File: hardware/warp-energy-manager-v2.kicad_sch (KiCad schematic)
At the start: 120 parts, among them J101 Boot, J102 DM3CS, P101 CON-SENSOR2, P102 SG-Ready, P103 L+N, P104 OUT, P105 INPUT, P110 MODBUS, P111 Debug, Q101 2N7002P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

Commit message: routing started
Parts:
- removed D101, D105, D107, D112: B0520LW-7, kicad-libraries:SOD-123, symbol tinkerforge:DIODESCH
- removed D104, D110: blue, kicad-libraries:D0603E, symbol tinkerforge:LED
- removed Q102, Q107: SSM6N7002KFU, kicad-libraries:SOT363, symbol tinkerforge:DUAL_MOSFET_N_CH
- removed R103, R114: 1k, kicad-libraries:R0603F, symbol tinkerforge:R
- removed RP105: 10k, kicad-libraries:4X0603, symbol tinkerforge:R_PACK4
- removed U105, U109: HCPL2731, kicad-libraries:DIP-8, symbol tinkerforge:HCPL-2731-000E
- added D101, D104, D105: LL4148, kicad-libraries:MiniMelf, symbol tinkerforge:DIODE
- added Q102, Q107: 2N7002P, kicad-libraries:SOT23GDS, symbol tinkerforge:MOSFET_N_CH
- added U106: IS2805-4, kicad-libraries:SOIC16_44, symbol tinkerforge:LTV-847
- C105: value 100uF -> 2.2uF; footprint kicad-libraries:C1210 -> kicad-libraries:C0603F
- P104: footprint kicad-libraries:OQ_4P_5mm -> kicad-libraries:OQ_4P_5mm_230V
- R101: value 1k -> 10k; footprint kicad-libraries:R1206E -> kicad-libraries:R0603F
- R102, R118: value 1k -> 10k
- R104, R105, R112, R115, R116, R117, R120, R121: footprint kicad-libraries:R1206E -> kicad-libraries:R0805E
- R110, R113: footprint kicad-libraries:R0402F -> kicad-libraries:R0603F
- U104: footprint (none) -> kicad-libraries:SOT25
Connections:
- net 3V3: now also RP104.2 (P2), RP104.3 (P3)
- net GND: now also D105.2 (K), Q102.S, Q107.S, U106.11, U106.13, U106.15, U106.9
- net IN0: now also RP104.8 (R1), U101.7 (P2.4_AI), U106.16; no longer RP104.2 (P2), U101.9 (P2.6_AI)
- net IN1: now also RP104.7 (R2), U101.8 (P2.5_AI), U106.14; no longer RP104.3 (P3), U101.10 (P2.7_AI)
- net L: now also U102.2 (N); no longer U102.1 (L)
- net N: now also U102.1 (L); no longer U102.2 (N)
- net RELAY0: now also Q107.G
- net RELAY1: now also Q102.G
- net V12: now also U101.6 (P2.3_AI); no longer U101.7 (P2.4_AI)
- net VCC: now also C115.2, D101.2 (K), D104.2 (K)
- net at R124.1: now also U101.12 (P2.9_AI); no longer U101.35 (P0.6_IO)
- net at C114.1, R112.2: now also U106.1
- net at C112.1, R117.2: now also U106.3
- net at L104.5, P110.1 (P1): no longer C115.2
- net at P110.2 (P2), R137.2: now also L104.6; no longer L104.7
- net at P110.3 (P3), R137.1: now also L104.7; no longer L104.6
- net at D111.1 (A), R134.2, R135.1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: now also L104.3; no longer L104.2
- net at D106.1 (A), R135.2, R136.1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: now also L104.2; no longer L104.3
- net at REL101.3: no longer P102.3 (P3)
- net at REL101.4: no longer P102.4 (P4)
- net at REL101.5: now also P102.4 (P4)
- net at REL101.6: now also P102.3 (P3)
- net at Q103.D, REL101.8: now also D104.1 (A)
- net at P102.1 (P1): now also REL102.6; no longer REL102.3
- net at P102.2 (P2): now also REL102.5; no longer REL102.4
- net at C134.1, R120.2: now also U106.5
- net at C124.1, R121.2: now also U106.7
- net IN2: now reaches RP104.6 (R3)
- net IN2: now also U101.9 (P2.6_AI), U106.12; no longer RP104.5 (R4)
- net at D108.1 (A), Q104.A1: now also Q102.D
- net at D109.1 (A), Q106.A1: now also Q107.D
- net at Q101.D, REL102.8: now also D101.1 (A)
- new net: D105.1 (A), U106.2, U106.4, U106.6, U106.8
- new net IN3: RP104.5 (R4), U101.10 (P2.7_AI), U106.10
- no-connect marks 29 -> 26
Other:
- note removed: "25mA max -> @12V -> 480 Ohm"
- moved on the sheet: C104, C107, C112, C113, C114, C115, C116, C122, C123, C124, C133, C134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

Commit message: fix schematic drcs
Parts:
- P111: footprint kicad-libraries:DEBUG_PAD -> kicad-libraries:TSTP_MINI
- U106: footprint kicad-libraries:SOIC16_44 -> DIP-16
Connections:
- net SD-CDS: now also U101.5 (P2.2_AI); no longer U101.4 (P2.1_AIO)
- net SD-EN: now also U101.4 (P2.1_AIO); no longer U101.25 (P1.1_IHO)
- no-connect marks 26 -> 25
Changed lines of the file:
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@@
 	)
 	(no_connect
-		(at 69.85 267.97)
-	)
-	(no_connect
-		(at 133.35 106.68)
+		(at 133.35 121.92)
 	)
 	(no_connect
-		(at 133.35 121.92)
+		(at 50.8 88.9)
 	)
 	(no_connect
@@
 	)
 	(no_connect
-		(at 69.85 265.43)
+		(at 133.35 88.9)
 	)
 	(no_connect
@@
 	)
 	(no_connect
+		(at 133.35 76.2)
+	)
+	(no_connect
 		(at 50.8 83.82)
 	)
@@
 		(at 133.35 148.59)
 	)
-	(no_connect
-		(at 69.85 262.89)
-	)
 	(wire
 		(pts
@@
 	(wire
 		(pts
-			(xy 133.35 104.14) (xy 130.81 104.14)
+			(xy 133.35 106.68) (xy 130.81 106.68)
 		)
 		(stroke
@@
 	(wire
 		(pts
-			(xy 129.54 76.2) (xy 133.35 76.2)
+			(xy 129.54 104.14) (xy 133.35 104.14)
 		)
 		(stroke
@@
 	(global_label "SD-EN"
 		(shape output)
-		(at 129.54 76.2 180)
+		(at 129.54 104.14 180)
 		(fields_autoplaced yes)
 		(effects
@@
 		)
 		(property "Intersheetrefs" "${INTERSHEET_REFS}"
-			(at 122.6274 76.2 0)
+			(at 122.6274 104.14 0)
 			(effects
 				(font
@@
 	(global_label "SD-CDS"
 		(shape input)
-		(at 130.81 104.14 180)
+		(at 130.81 106.68 180)
 		(fields_autoplaced yes)
 		(effects
@@
 		)
 		(property "Intersheetrefs" "${INTERSHEET_REFS}"
-			(at 122.9069 104.14 0)
+			(at 122.9069 106.68 0)
 			(effects
 				(font
@@
 			)
 		)
-		(property "Description" ""
+		(property "Description" "Connector 01x02"
 			(at 19.05 68.58 0)
 			(effects
@@
 			)
 		)
-		(property "Description" ""
+		(property "Description" "4 resistors Pack"
 			(at 124.46 46.99 0)
 			(effects
@@
 			)
 		)
-		(property "Footprint" "kicad-libraries:DEBUG_PAD"
+		(property "Footprint" "kicad-libraries:TSTP_MINI"
 			(at 43.18 78.74 0)
 			(effects
@@
 			)
 		)
-		(property "Description" ""
+		(property "Description" "Transistor P-MOSFET (general)"
 			(at 99.06 33.02 0)
 			(effects
@@
 			)
 		)
-		(property "Description" ""
+		(property "Description" "Connector 01x04"
 			(at 130.81 251.46 0)
 			(effects
@@
 			)
 		)
-		(property "Description" ""
+		(property "Description" "power-flag symbol"
 			(at 224.79 172.72 0)
 			(effects
@@
 			)
 		)
-		(property "Description" ""
+		(property "Description" "4 resistors Pack"
 			(at 39.37 255.27 0)
 			(effects
@@
 	)
 	(symbol
-		(lib_name "CONN_01X04_1")
 		(lib_id "tinkerforge:CONN_01X04")
 		(at 167.64 114.3 180)
@@
 			)
 		)
-		(property "Description" ""
+		(property "Description" "power-flag symbol"
 			(at 91.44 93.98 0)
 			(effects
@@
 			)
 		)
-		(property "Description" ""
+		(property "Description" "Transistor P-MOSFET, collector connected to mounting plane (general)"
 			(at 232.41 38.1 0)
 			(effects
@@
 			)
 		)
-		(property "Description" ""
+		(property "Description" "power-flag symbol"
 			(at 207.01 39.37 0)
 			(effects
@@
 			)
 		)
-		(property "Description" ""
+		(property "Description" "4 resistors Pack"
 			(at 367.03 219.71 0)
 			(effects
@@
 			)
 		)
-		(property "Description" ""
+		(property "Description" "power-flag symbol"
 			(at 119.38 229.87 0)
 			(effects
@@
 			)
 		)
-		(property "Description" ""
+		(property "Description" "Transistor P-MOSFET, collector connected to mounting plane (general)"
 			(at 302.26 45.72 0)
 			(effects
@@
 	)
 	(symbol
-		(lib_name "CONN_01X04_1")
 		(lib_id "tinkerforge:CONN_01X04")
 		(at 167.64 54.61 180)
@@
 			)
 		)
-		(property "Description" ""
+		(property "Description" "power-flag symbol"
 			(at 100.33 207.01 0)
 			(effects
@@
 			)
 		)
-		(property "Description" ""
+		(property "Description" "power-flag symbol"
 			(at 207.01 78.74 0)
 			(effects
@@
 			)
 		)
-		(property "Footprint" "kicad-libraries:SOIC16_44"
+		(property "Footprint" "DIP-16"
 			(at 266.7 191.4355 0)
 			(effects
@@
 			)
 		)
-		(property "Datasheet" ""
+		(property "Datasheet" "http://www.us.liteon.com/downloads/LTV-817-827-847.PDF"
 			(at 266.7 193.8598 0)
 			(effects
@@
 			)
 		)
-		(property "Description" ""
+		(property "Description" "DIP-16, Quad DC Optocoupler, Vce 35V, CTR 50%"
 			(at 266.7 212.09 0)
 			(effects
@@
 			)
 		)
-		(property "Description" ""
+		(property "Description" "Transistor P-MOSFET, collector connected to mounting plane (general)"
 			(at 302.26 95.25 0)
 			(effects
@@
 			)
 		)
-		(property "Description" ""
+		(property "Description" "Transistor P-MOSFET, collector connected to mounting plane (general)"
 			(at 232.41 77.47 0)
 			(effects
@@
 			)
 		)
-		(property "Description" ""
+		(property "Description" "power-flag symbol"
 			(at 304.8 71.12 0)
 			(effects
@@
 			)
 		)
-		(property "Description" ""
+		(property "Description" "4 resistors Pack"
 			(at 290.83 189.23 0)
 			(effects
@@
 			)
 		)
-		(property "Description" ""
+		(property "Description" "power-flag symbol"
 			(at 304.8 21.59 0)
 			(effects
@@
 			)
 		)
-		(property "Description" ""
+		(property "Description" "power-flag symbol"
 			(at 224.79 218.44 0)
 			(effects

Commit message: fully routed
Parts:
- P111: footprint kicad-libraries:TSTP_MINI -> kicad-libraries:TSTP_STL
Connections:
- net RELAY0: now also U101.24 (P1.2_IHO); no longer U101.22 (P1.4_IHO)
- net RELAY1: now also U101.23 (P1.3_IHO); no longer U101.21 (P1.5_IHO)
- net SG-OUT-0: now also U101.22 (P1.4_IHO); no longer U101.24 (P1.2_IHO)
- net SG-OUT-1: now also U101.21 (P1.5_IHO); no longer U101.23 (P1.3_IHO)
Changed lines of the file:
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@@
 	(global_label "RELAY1"
 		(shape output)
-		(at 129.54 86.36 180)
-		(fields_autoplaced yes)
-		(effects
-			(font
-				(size 0.9906 0.9906)
-			)
-			(justify right)
-		)
-		(property "Intersheetrefs" "${INTERSHEET_REFS}"
-			(at 122.3916 86.36 0)
+		(at 129.54 81.28 180)
+		(fields_autoplaced yes)
+		(effects
+			(font
+				(size 0.9906 0.9906)
+			)
+			(justify right)
+		)
+		(property "Intersheetrefs" "${INTERSHEET_REFS}"
+			(at 122.3916 81.28 0)
 			(effects
 				(font
@@
 	(global_label "SG-OUT-0"
 		(shape output)
-		(at 129.54 78.74 180)
-		(fields_autoplaced yes)
-		(effects
-			(font
-				(size 0.9906 0.9906)
-			)
-			(justify right)
-		)
-		(property "Intersheetrefs" "${INTERSHEET_REFS}"
-			(at 119.5613 78.74 0)
+		(at 129.54 83.82 180)
+		(fields_autoplaced yes)
+		(effects
+			(font
+				(size 0.9906 0.9906)
+			)
+			(justify right)
+		)
+		(property "Intersheetrefs" "${INTERSHEET_REFS}"
+			(at 119.5613 83.82 0)
 			(effects
 				(font
@@
 	(global_label "RELAY0"
 		(shape output)
-		(at 129.54 83.82 180)
-		(fields_autoplaced yes)
-		(effects
-			(font
-				(size 0.9906 0.9906)
-			)
-			(justify right)
-		)
-		(property "Intersheetrefs" "${INTERSHEET_REFS}"
-			(at 122.3916 83.82 0)
+		(at 129.54 78.74 180)
+		(fields_autoplaced yes)
+		(effects
+			(font
+				(size 0.9906 0.9906)
+			)
+			(justify right)
+		)
+		(property "Intersheetrefs" "${INTERSHEET_REFS}"
+			(at 122.3916 78.74 0)
 			(effects
 				(font
@@
 	(global_label "SG-OUT-1"
 		(shape output)
-		(at 129.54 81.28 180)
-		(fields_autoplaced yes)
-		(effects
-			(font
-				(size 0.9906 0.9906)
-			)
-			(justify right)
-		)
-		(property "Intersheetrefs" "${INTERSHEET_REFS}"
-			(at 119.5613 81.28 0)
+		(at 129.54 86.36 180)
+		(fields_autoplaced yes)
+		(effects
+			(font
+				(size 0.9906 0.9906)
+			)
+			(justify right)
+		)
+		(property "Intersheetrefs" "${INTERSHEET_REFS}"
+			(at 119.5613 86.36 0)
 			(effects
 				(font
@@
 			)
 		)
-		(property "Footprint" "kicad-libraries:TSTP_MINI"
+		(property "Footprint" "kicad-libraries:TSTP_STL"
 			(at 43.18 78.74 0)
 			(effects

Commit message: all bugs fixed
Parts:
- U106: footprint DIP-16 -> kicad-libraries:SOIC16_44
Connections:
- net at P111.1: now also U101.35 (P0.6_IO); no longer U101.31 (P0.2_IO)
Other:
- moved on the sheet: P111
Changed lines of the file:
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@@
 	)
 	(no_connect
-		(at 50.8 88.9)
+		(at 50.8 78.74)
 	)
 	(no_connect
@@
 	(wire
 		(pts
-			(xy 50.8 78.74) (xy 45.72 78.74)
+			(xy 50.8 88.9) (xy 45.72 88.9)
 		)
 		(stroke
@@
 	(symbol
 		(lib_id "tinkerforge:CONN_1")
-		(at 43.18 78.74 0)
+		(at 43.18 88.9 0)
 		(mirror y)
 		(unit 1)
@@
 		(dnp no)
 		(property "Reference" "P111"
-			(at 49.53 77.47 0)
+			(at 40.64 86.36 0)
 			(effects
 				(font
@@
 		)
 		(property "Value" "Debug"
-			(at 38.1 78.74 0)
+			(at 38.1 88.9 0)
 			(effects
 				(font
@@
 		)
 		(property "Footprint" "kicad-libraries:TSTP_STL"
-			(at 43.18 78.74 0)
+			(at 43.18 88.9 0)
 			(effects
 				(font
@@
 		)
 		(property "Datasheet" ""
-			(at 43.18 78.74 0)
+			(at 43.18 88.9 0)
 			(effects
 				(font
@@
 		)
 		(property "Description" ""
-			(at 43.18 78.74 0)
+			(at 43.18 88.9 0)
 			(effects
 				(font
@@
 			)
 		)
-		(property "Footprint" "DIP-16"
+		(property "Footprint" "kicad-libraries:SOIC16_44"
 			(at 266.7 191.4355 0)
 			(effects
@@
 			)
 		)
-		(property "Datasheet" "http://www.us.liteon.com/downloads/LTV-817-827-847.PDF"
+		(property "Datasheet" ""
 			(at 266.7 193.8598 0)
 			(effects
@@
 			)
 		)
-		(property "Description" "DIP-16, Quad DC Optocoupler, Vce 35V, CTR 50%"
+		(property "Description" ""
 			(at 266.7 212.09 0)
 			(effects

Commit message: add 3d models
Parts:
- R104, R105, R115, R116: value 1k -> 2k2
- R112, R117, R120, R121: value 1k -> 680
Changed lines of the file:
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@@
 			)
 		)
-		(property "Value" "1k"
+		(property "Value" "680"
 			(at 214.63 184.15 90)
 			(effects
@@
 			)
 		)
-		(property "Value" "1k"
+		(property "Value" "680"
 			(at 214.63 191.77 90)
 			(effects
@@
 			)
 		)
-		(property "Value" "1k"
+		(property "Value" "2k2"
 			(at 185.42 199.39 90)
 			(effects
@@
 			)
 		)
-		(property "Value" "1k"
+		(property "Value" "2k2"
 			(at 180.34 199.39 90)
 			(effects
@@
 			)
 		)
-		(property "Value" "1k"
+		(property "Value" "2k2"
 			(at 180.34 245.11 90)
 			(effects
@@
 			)
 		)
-		(property "Value" "1k"
+		(property "Value" "2k2"
 			(at 185.42 245.11 90)
 			(effects
@@
 			)
 		)
-		(property "Value" "1k"
+		(property "Value" "680"
 			(at 214.63 229.87 90)
 			(effects
@@
 			)
 		)
-		(property "Value" "1k"
+		(property "Value" "680"
 			(at 214.63 237.49 90)
 			(effects

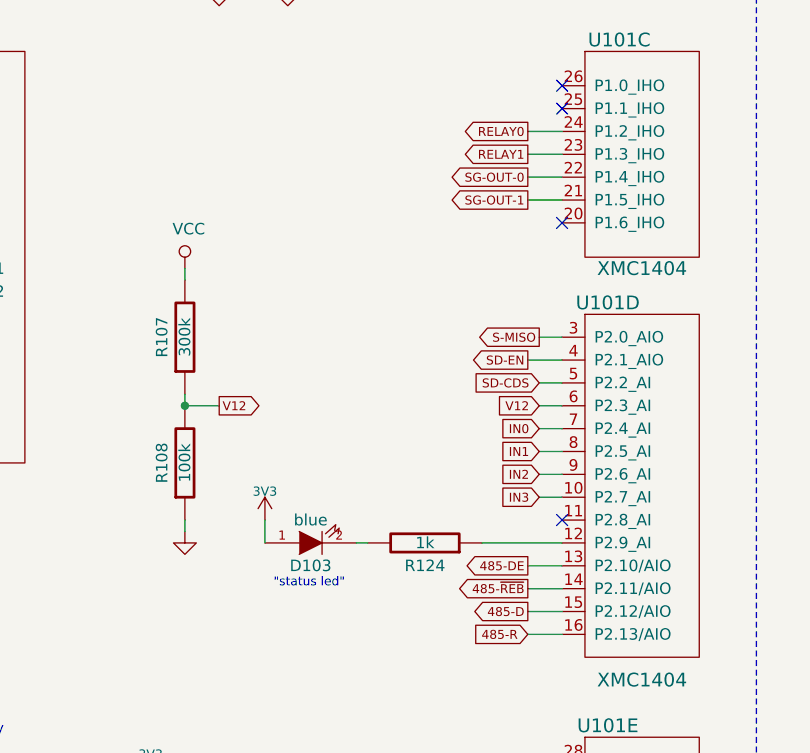
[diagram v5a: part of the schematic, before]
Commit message: add version 2.1: fix varistor space, fix status led
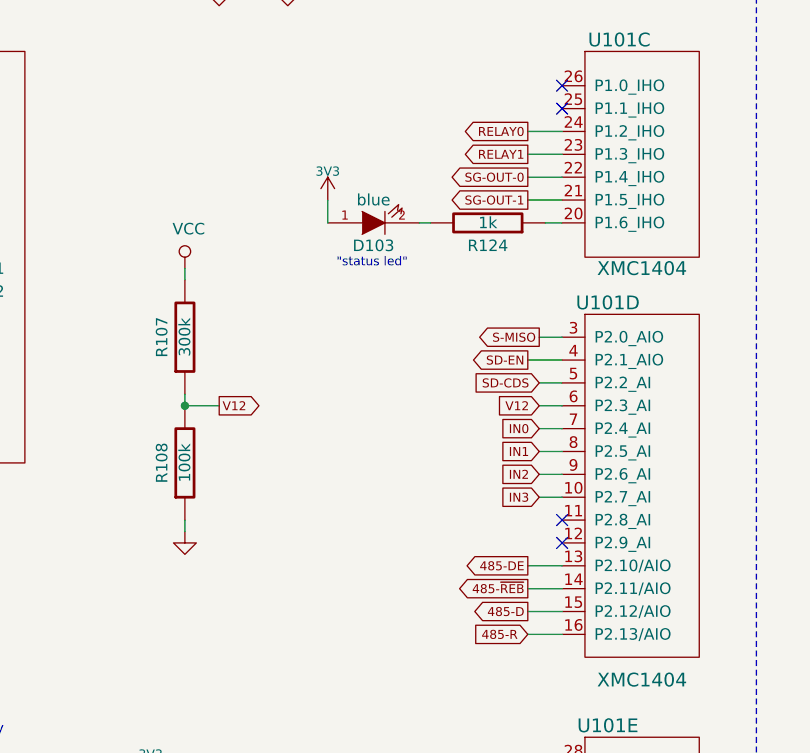
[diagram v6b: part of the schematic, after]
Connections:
- net at R124.1: now also U101.20 (P1.6_IHO); no longer U101.12 (P2.9_AI)
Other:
- moved on the sheet: D103, R124
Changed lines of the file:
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@@
 	(title_block
 		(title "Energy Manager Bricklet")
-		(date "2024-06-17")
-		(rev "2.0")
+		(date "2024-07-17")
+		(rev "2.1")
 		(company "Tinkerforge GmbH")
 		(comment 1 "Licensed under CERN OHL v.1.1")
@@
 	)
 	(no_connect
-		(at 133.35 88.9)
-	)
-	(no_connect
 		(at 196.85 69.85)
 	)
@@
 	)
 	(no_connect
+		(at 133.35 124.46)
+	)
+	(no_connect
 		(at 201.93 22.86)
 	)
@@
 	(wire
 		(pts
-			(xy 100.33 121.92) (xy 100.33 124.46)
+			(xy 107.315 86.36) (xy 107.315 88.9)
 		)
 		(stroke
@@
 	(wire
 		(pts
+			(xy 131.445 88.9) (xy 133.35 88.9)
+		)
+		(stroke
+			(width 0)
+			(type default)
+		)
+	)
+	(wire
+		(pts
 			(xy 264.16 33.02) (xy 264.16 113.03)
 		)
@@
 	(wire
 		(pts
-			(xy 124.46 124.46) (xy 133.35 124.46)
-		)
-		(stroke
-			(width 0)
-			(type default)
-		)
-	)
-	(wire
-		(pts
 			(xy 219.71 21.59) (xy 219.71 20.32)
 		)
@@
 	(wire
 		(pts
-			(xy 110.49 124.46) (xy 111.76 124.46)
+			(xy 117.475 88.9) (xy 118.745 88.9)
 		)
 		(stroke
@@
 	(text "\"status led\""
 		(exclude_from_sim no)
-		(at 109.22 129.54 0)
+		(at 116.205 93.98 0)
 		(effects
 			(font
@@
 	(symbol
 		(lib_id "tinkerforge:LED")
-		(at 105.41 124.46 0)
+		(at 112.395 88.9 0)
 		(mirror x)
 		(unit 1)
@@
 		(dnp no)
 		(property "Reference" "D103"
-			(at 105.41 127 0)
+			(at 112.395 91.44 0)
 			(effects
 				(font
@@
 		)
 		(property "Value" "blue"
-			(at 105.41 121.92 0)
+			(at 112.395 86.36 0)
 			(effects
 				(font
@@
 		)
 		(property "Footprint" "kicad-libraries:D0603F"
-			(at 105.41 124.46 0)
+			(at 112.395 88.9 0)
 			(effects
 				(font
@@
 		)
 		(property "Datasheet" ""
-			(at 105.41 124.46 0)
+			(at 112.395 88.9 0)
 			(effects
 				(font
@@
 		)
 		(property "Description" ""
-			(at 105.41 124.46 0)
+			(at 112.395 88.9 0)
 			(effects
 				(font
@@
 	(symbol
 		(lib_id "tinkerforge:3V3")
-		(at 100.33 121.92 0)
+		(at 107.315 86.36 0)
 		(mirror y)
 		(unit 1)
@@
 		(dnp no)
 		(property "Reference" "#PWR0106"
-			(at 100.33 119.38 0)
+			(at 107.315 83.82 0)
 			(effects
 				(font
@@
 		)
 		(property "Value" "3V3"
-			(at 100.33 118.745 0)
+			(at 107.315 83.185 0)
 			(effects
 				(font
@@
 		)
 		(property "Footprint" ""
-			(at 100.33 121.92 0)
+			(at 107.315 86.36 0)
 			(effects
 				(font
@@
 		)
 		(property "Datasheet" ""
-			(at 100.33 121.92 0)
+			(at 107.315 86.36 0)
 			(effects
 				(font
@@
 		)
 		(property "Description" ""
-			(at 100.33 121.92 0)
+			(at 107.315 86.36 0)
 			(effects
 				(font
@@
 	(symbol
 		(lib_id "tinkerforge:R")
-		(at 118.11 124.46 270)
+		(at 125.095 88.9 270)
 		(mirror x)
 		(unit 1)
@@
 		(dnp no)
 		(property "Reference" "R124"
-			(at 118.11 127 90)
+			(at 125.095 91.44 90)
 			(effects
 				(font
@@
 		)
 		(property "Value" "1k"
-			(at 118.11 124.46 90)
+			(at 125.095 88.9 90)
 			(effects
 				(font
@@
 		)
 		(property "Footprint" "kicad-libraries:R0603F"
-			(at 118.11 124.46 0)
+			(at 125.095 88.9 0)
 			(effects
 				(font
@@
 		)
 		(property "Datasheet" ""
-			(at 118.11 124.46 0)
+			(at 125.095 88.9 0)
 			(effects
 				(font
@@
 		)
 		(property "Description" ""
-			(at 118.11 124.46 0)
+			(at 125.095 88.9 0)
 			(effects
 				(font

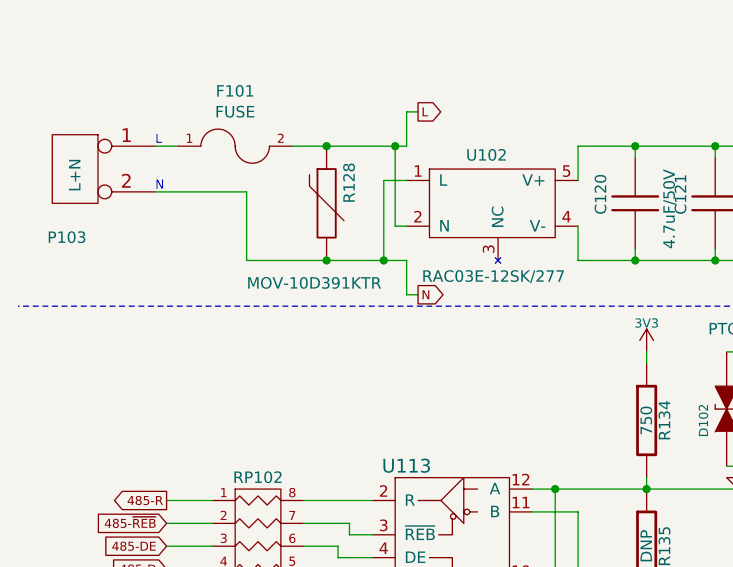
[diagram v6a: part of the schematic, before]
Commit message: change varistor value
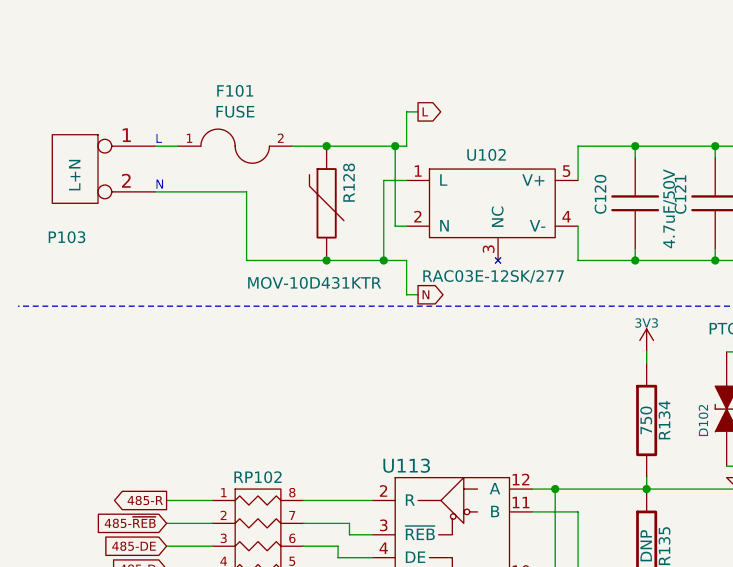
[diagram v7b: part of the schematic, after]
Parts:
- R128: value MOV-10D391KTR -> MOV-10D431KTR
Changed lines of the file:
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@@
 			)
 		)
-		(property "Value" "MOV-10D391KTR"
+		(property "Value" "MOV-10D431KTR"
 			(at 38.1 222.25 0)
 			(effects
